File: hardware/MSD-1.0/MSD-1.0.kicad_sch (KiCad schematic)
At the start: 19 parts, among them J1 Conn_01x05, J2 Conn_01x03, Q1 IRF840N, U1 NE555P, U2 PC817, U3 PC817

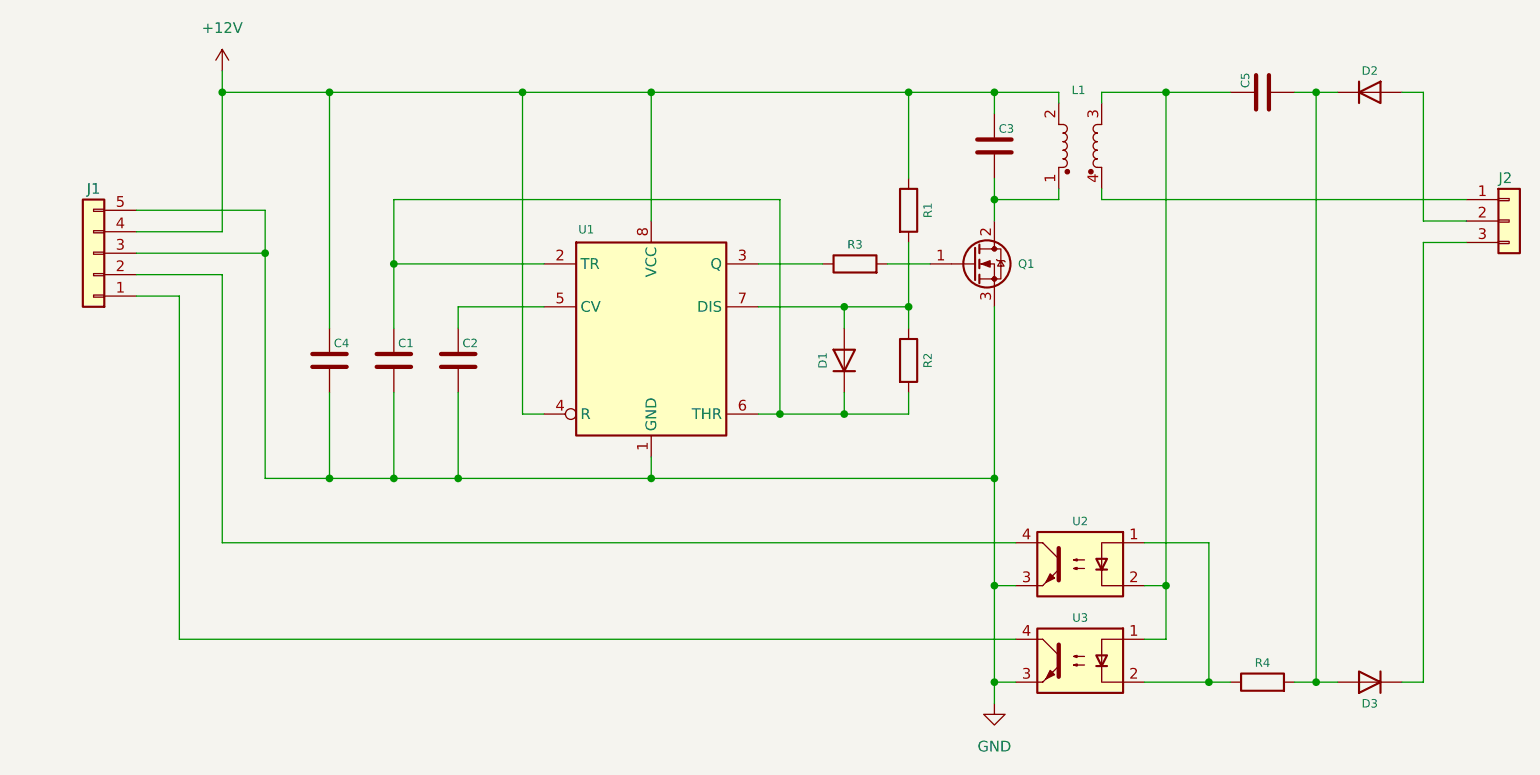
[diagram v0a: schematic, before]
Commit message: deleted:    hardware/MSD-1.0/#auto_saved_files# 	new file:   hardware/MSD-1.0/MSD-1.0 BoM.csv 	new file:   hardware/MSD-1.0/MSD-1.0-B_Cu.gbr 	new file:   hardware/MSD-1.0/MSD-1.0-B_Mask.gbr 	new file:   hardware/MSD-1.0/MSD-1.0-B_Paste.gbr 	new file:   hardware/MSD-1.0/MSD-1.0-B_Silkscreen.gbr 	new file:   hardware/MSD-1.0/MSD-1.0-Edge_Cuts.gbr 	new file:   hardware/MSD-1.0/MSD-1.0-F_Cu.gbr 	new file:   hardware/MSD-1.0/MSD-1.0-F_Mask.gbr 	new file:   hardware/MSD-1.0/MSD-1.0-F_Paste.gbr 	new file:   hardware/MSD-1.0/MSD-1.0-F_Silkscreen.gbr 	new file:   hardware/MSD-1.0/MSD-1.0-NPTH.drl 	new file:   hardware/MSD-1.0/MSD-1.0-PTH.drl 	deleted:    hardware/MSD-1.0/MSD-1.0-backups/MSD-1.0-2025-02-24_160102.zip 	deleted:    hardware/MSD-1.0/MSD-1.0-backups/MSD-1.0-2025-02-24_160721.zip 	deleted:    hardware/MSD-1.0/MSD-1.0-backups/MSD-1.0-2025-02-24_161316.zip 	deleted:    hardware/MSD-1.0/MSD-1.0-backups/MSD-1.0-2025-02-24_162407.zip 	deleted:    hardware/MSD-1.0/MSD-1.0-backups/MSD-1.0-2025-02-24_163137.zip 	deleted:    hardware/MSD-1.0/MSD-1.0-backups/MSD-1.0-2025-02-25_161045.zip 	deleted:    hardware/MSD-1.0/MSD-1.0-backups/MSD-1.0-2025-02-26_093224.zip 	deleted:    hardware/MSD-1.0/MSD-1.0-backups/MSD-1.0-2025-02-26_094218.zip 	new file:   hardware/MSD-1.0/MSD-1.0-backups/MSD-1.0-2025-02-26_163854.zip 	new file:   hardware/MSD-1.0/MSD-1.0-backups/MSD-1.0-2025-02-27_112851.zip 	new file:   hardware/MSD-1.0/MSD-1.0-backups/MSD-1.0-2025-02-27_114053.zip 	new file:   hardware/MSD-1.0/MSD-1.0-backups/MSD-1.0-2025-02-27_185834.zip 	new file:   hardware/MSD-1.0/MSD-1.0-backups/MSD-1.0-2025-02-27_190654.zip 	new file:   hardware/MSD-1.0/MSD-1.0-backups/MSD-1.0-2025-02-27_191228.zip 	new file:   hardware/MSD-1.0/MSD-1.0-backups/MSD-1.0-2025-02-28_140545.zip 	new file:   hardware/MSD-1.0/MSD-1.0-backups/MSD-1.0-2025-02-28_141533.zip 	new file:   hardware/MSD-1.0/MSD-1.0-backups/MSD-1.0-2025-02-28_142536.zip 	new file:   hardware/MSD-1.0/MSD-1.0-backups/MSD-1.0-2025-02-28_14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
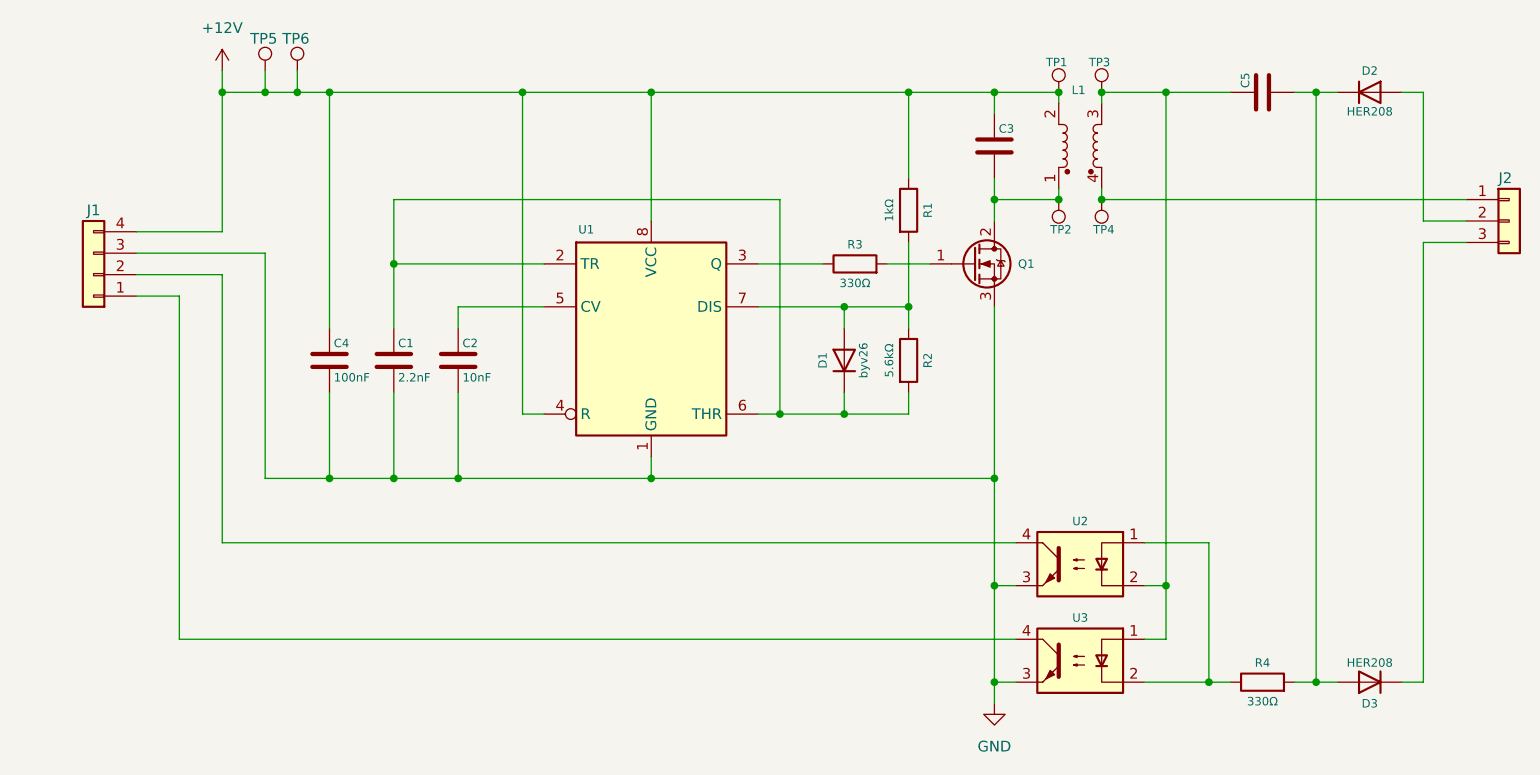
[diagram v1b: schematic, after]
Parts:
- added TP1, TP2, TP3, TP4: TestPoint, TestPoint:TestPoint_Bridge_Pitch2.54mm_Drill1.0mm, symbol Connector:TestPoint
- added TP5, TP6: TestPoint, TestPoint:TestPoint_THTPad_2.0x2.0mm_Drill1.0mm_NoSilkscreen, symbol Connector:TestPoint
- C2: value 470pF -> 10nF
- C3: value 0.022uF 275V MKP -> 0.022uF 400V MKP
- C4: value C -> 100nF
- C5: value 10nF -> ~; footprint Capacitor_THT:C_Rect_L7.0mm_W3.5mm_P5.00mm -> Capacitor_THT:C_Rect_L13.0mm_W5.0mm_P10.00mm_FKS3_FKP3_MKS4
- D2, D3: value D -> HER208
- J1: footprint Connector_PinHeader_2.54mm:PinHeader_1x05_P2.54mm_Horizontal -> Connector_PinHeader_2.54mm:PinHeader_1x04_P2.54mm_Horizontal_Custom; symbol Connector_Generic:Conn_01x05 -> Connector_Generic:Conn_01x04
- J2: footprint Connector_PinHeader_2.54mm:PinHeader_1x03_P5.08mm_Horizontal -> Connector_PinHeader_2.54mm:PinHeader_1x03_P5.08mm_Horizontal_Custom
- L1: value L_Coupled -> Isolation Transformer (Custom)
- Q1: value IRF840N -> IRF840
- R1: value 10kΩ -> 1kΩ
- R4: value R -> 330Ω
- U1: footprint Package_DIP:DIP-8_W7.62mm -> Package_DIP:DIP-8_W7.62mm_Socket
- U2, U3: footprint Package_DIP:DIP-4_W7.62mm -> Package_DIP:DIP-4_W7.62mm_Socket
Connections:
- net +12V: now also TP1.1, TP5.1, TP6.1
- net GND: no longer J1.5 (Pin_5)
- net at C3.2, L1.1, Q1.2 (D): now also TP2.1
- net at J2.1 (Pin_1), L1.4: now also TP4.1
- net at C5.1, L1.3, U2.2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: now also TP3.1

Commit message: modified:   .DS_Store 	deleted:    hardware/MSD-1.0/MSD-1.0-backups/MSD-1.0-2025-02-25_161819.zip 	deleted:    hardware/MSD-1.0/MSD-1.0-backups/MSD-1.0-2025-02-25_162448.zip 	deleted:    hardware/MSD-1.0/MSD-1.0-backups/MSD-1.0-2025-02-25_163016.zip 	deleted:    hardware/MSD-1.0/MSD-1.0-backups/MSD-1.0-2025-02-25_163954.zip 	deleted:    hardware/MSD-1.0/MSD-1.0-backups/MSD-1.0-2025-02-26_112856.zip 	deleted:    hardware/MSD-1.0/MSD-1.0-backups/MSD-1.0-2025-02-26_113923.zip 	deleted:    hardware/MSD-1.0/MSD-1.0-backups/MSD-1.0-2025-02-26_115654.zip 	deleted:    hardware/MSD-1.0/MSD-1.0-backups/MSD-1.0-2025-02-26_120757.zip 	deleted:    hardware/MSD-1.0/MSD-1.0-backups/MSD-1.0-2025-02-26_163854.zip 	deleted:    hardware/MSD-1.0/MSD-1.0-backups/MSD-1.0-2025-02-27_112851.zip 	deleted:    hardware/MSD-1.0/MSD-1.0-backups/MSD-1.0-2025-02-27_114053.zip 	deleted:    hardware/MSD-1.0/MSD-1.0-backups/MSD-1.0-2025-02-27_185834.zip 	deleted:    hardware/MSD-1.0/MSD-1.0-backups/MSD-1.0-2025-02-27_190654.zip 	deleted:    hardware/MSD-1.0/MSD-1.0-backups/MSD-1.0-2025-02-27_191228.zip 	deleted:    hardware/MSD-1.0/MSD-1.0-backups/MSD-1.0-2025-02-28_140545.zip 	deleted:    hardware/MSD-1.0/MSD-1.0-backups/MSD-1.0-2025-02-28_141533.zip 	deleted:    hardware/MSD-1.0/MSD-1.0-backups/MSD-1.0-2025-02-28_142536.zip 	deleted:    hardware/MSD-1.0/MSD-1.0-backups/MSD-1.0-2025-02-28_143342.zip 	deleted:    hardware/MSD-1.0/MSD-1.0-backups/MSD-1.0-2025-02-28_162722.zip 	deleted:    hardware/MSD-1.0/MSD-1.0-backups/MSD-1.0-2025-03-05_134102.zip 	deleted:    hardware/MSD-1.0/MSD-1.0-backups/MSD-1.0-2025-03-05_134620.zip 	new file:   hardware/MSD-1.0/MSD-1.0-backups/MSD-1.0-2025-03-24_113503.zip 	new file:   hardware/MSD-1.0/MSD-1.0-backups/MSD-1.0-2025-03-24_114029.zip 	new file:   hardware/MSD-1.0/MSD-1.0-backups/MSD-1.0-2025-03-24_132745.zip 	new file:   hardware/MSD-1.0/MSD-1.0-backups/MSD-1.0-2025-03-24_134332.zip 	new file:   hardware/MSD-1.0/MSD-1.0-backups/MSD-1.0-2025-03-25_144744.zip 	n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
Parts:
- removed L1: Isolation Transformer (Custom), Inductor_THT:L_CommonMode_Toroid_Vertical_L30.5mm_W15.2mm_Px10.16mm_Py20.32mm_Bourns_8100, symbol Device:L_Coupled_1243
- added C6: 470µF 35V, Capacitor_THT:CP_Radial_D12.5mm_P5.00mm, symbol Device:C_Polarized
- added L1: L_Ferrite_Coupled, Inductor_THT:L_CommonMode_Toroid_Horizontal_OD23mm_ID14mm_H8mm, symbol Device:L_Ferrite_Coupled_1243
- D1: footprint Diode_THT:D_DO-34_SOD68_P7.62mm_Horizontal -> Diode_THT:D_DO-35_SOD27_P7.62mm_Horizontal
- J1: footprint Connector_PinHeader_2.54mm:PinHeader_1x04_P2.54mm_Horizontal_Custom -> Connector_PinHeader_2.54mm:PinHeader_1x04_P2.54mm_Horizontal_2
- J2: footprint Connector_PinHeader_2.54mm:PinHeader_1x03_P5.08mm_Horizontal_Custom -> Connector_PinHeader_2.54mm:PinHeader_1x03_P5.08mm_Horizontal_2
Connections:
- net +12V: now also C6.1, L1.2
- net GND: now also C6.2
- net at C3.2, Q1.2 (D), TP2.1: now also L1.1
- net at J2.1 (Pin_1), TP4.1: now also L1.4
- net at C5.1, TP3.1, U2.2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: now also L1.3
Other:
- moved on the sheet: J1, TP1, TP2, TP3, TP4, TP6

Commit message: new file:   hardware/Gain/Gain-B_Cu.gbr 	new file:   hardware/Gain/Gain-B_Mask.gbr 	new file:   hardware/Gain/Gain-B_Paste.gbr 	new file:   hardware/Gain/Gain-B_Silkscreen.gbr 	new file:   hardware/Gain/Gain-Edge_Cuts.gbr 	new file:   hardware/Gain/Gain-F_Cu.gbr 	new file:   hardware/Gain/Gain-F_Mask.gbr 	new file:   hardware/Gain/Gain-F_Paste.gbr 	new file:   hardware/Gain/Gain-F_Silkscreen.gbr 	new file:   hardware/Gain/Gain-NPTH.drl 	new file:   hardware/Gain/Gain-PTH.drl 	new file:   hardware/Gain/Gain-backups/Gain-2025-04-14_115147.zip 	new file:   hardware/Gain/Gain-backups/Gain-2025-04-14_121847.zip 	new file:   hardware/Gain/Gain-backups/Gain-2025-04-14_133755.zip 	new file:   hardware/Gain/Gain-backups/Gain-2025-04-14_141907.zip 	new file:   hardware/Gain/Gain-backups/Gain-2025-04-14_162042.zip 	new file:   hardware/Gain/Gain-backups/Gain-2025-04-14_163456.zip 	new file:   hardware/Gain/Gain-job.gbrjob 	new file:   hardware/Gain/Gain.kicad_pcb 	new file:   hardware/Gain/Gain.kicad_prl 	new file:   hardware/Gain/Gain.kicad_pro 	new file:   hardware/Gain/Gain.kicad_sch 	new file:   hardware/Gain/Gain.step 	new file:   hardware/Gain/REM-2.0 BoM.csv 	new file:   hardware/Gain/REM-2.0-backups/REM-2.0-2025-03-05_160217.zip 	new file:   hardware/Gain/REM-2.0-backups/REM-2.0-2025-03-06_081735.zip 	new file:   hardware/Gain/REM-2.0-backups/REM-2.0-2025-03-17_111724.zip 	new file:   hardware/Gain/REM-2.0-backups/REM-2.0-2025-03-17_135033.zip 	new file:   hardware/Gain/REM-2.0-backups/REM-2.0-2025-03-18_104019.zip 	new file:   hardware/Gain/REM-2.0-backups/REM-2.0-2025-03-18_141720.zip 	new file:   hardware/Gain/REM-2.0-backups/REM-2.0-2025-03-18_202240.zip 	new file:   hardware/Gain/REM-2.0-backups/REM-2.0-2025-03-18_203414.zip 	new file:   hardware/Gain/REM-2.0-backups/REM-2.0-2025-03-18_204444.zip 	new file:   hardware/Gain/REM-2.0-backups/REM-2.0-2025-03-24_102406.zip 	new file:   hardware/Gain/REM-2.0-backups/REM-2.0-2025-03-24_103843.zip 	new file:   hardware/Ga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
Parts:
- C5: value ~ -> 100nF 400V
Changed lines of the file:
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@@
 			)
 		)
-		(property "Value" "~"
+		(property "Value" "100nF 400V"
 			(at 167.132 31.242 0)
 			(effects
@@
 				)
 				(justify left)
+				(hide yes)
 			)
 		)

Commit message: deleted:    hardware/Gain/Gain-backups/Gain-2025-04-14_115147.zip 	new file:   hardware/Gain/Gain-backups/Gain-2025-04-15_120154.zip 	deleted:    hardware/MSD-1.0/MSD-1.0-backups/MSD-1.0-2025-03-24_134332.zip 	deleted:    hardware/MSD-1.0/MSD-1.0-backups/MSD-1.0-2025-03-25_144744.zip 	deleted:    hardware/MSD-1.0/MSD-1.0-backups/MSD-1.0-2025-03-25_145433.zip 	deleted:    hardware/MSD-1.0/MSD-1.0-backups/MSD-1.0-2025-03-25_150210.zip 	deleted:    hardware/MSD-1.0/MSD-1.0-backups/MSD-1.0-2025-03-25_150818.zip 	new file:   hardware/MSD-1.0/MSD-1.0-backups/MSD-1.0-2025-04-16_142822.zip 	new file:   hardware/MSD-1.0/MSD-1.0-backups/MSD-1.0-2025-04-16_143722.zip 	new file:   hardware/MSD-1.0/MSD-1.0-backups/MSD-1.0-2025-04-16_145208.zip 	new file:   hardware/MSD-1.0/MSD-1.0-backups/MSD-1.0-2025-04-16_150237.zip 	new file:   hardware/MSD-1.0/MSD-1.0-backups/MSD-1.0-2025-04-16_150829.zip 	modified:   hardware/MSD-1.0/MSD-1.0.kicad_pcb 	modified:   hardware/MSD-1.0/MSD-1.0.kicad_sch 	modified:   hardware/MSD-1.0/MSD-1.0.step 	new file:   hardware/MSD-2.0/MSD-2.0-backups/MSD-2.0-2025-04-16_090248.zip 	deleted:    hardware/PS-1.0/PS-1.0-backups/PS-1.0-2025-03-18_205016.zip 	deleted:    hardware/PS-1.0/PS-1.0-backups/PS-1.0-2025-03-18_205728.zip 	deleted:    hardware/PS-1.0/PS-1.0-backups/PS-1.0-2025-03-18_211157.zip 	deleted:    hardware/PS-1.0/PS-1.0-backups/PS-1.0-2025-03-18_213933.zip 	deleted:    hardware/PS-1.0/PS-1.0-backups/PS-1.0-2025-03-19_094557.zip 	deleted:    hardware/PS-1.0/PS-1.0-backups/PS-1.0-2025-03-19_101204.zip 	deleted:    hardware/PS-1.0/PS-1.0-backups/PS-1.0-2025-03-19_102323.zip 	new file:   hardware/PS-1.0/PS-1.0-backups/PS-1.0-2025-04-16_154157.zip 	new file:   hardware/PS-1.0/PS-1.0-backups/PS-1.0-2025-04-16_154838.zip 	new file:   hardware/PS-1.0/PS-1.0-backups/PS-1.0-2025-04-16_155906.zip 	new file:   hardware/PS-1.0/PS-1.0-backups/PS-1.0-2025-04-16_160456.zip 	new file:   hardware/PS-1.0/PS-1.0-backups/PS-1.0-2025-04-16_161300.zip 	new file:   har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
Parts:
- added TP7: TestPoint, TestPoint:TestPoint_Bridge_Pitch2.54mm_Drill1.0mm, symbol Connector:TestPoint
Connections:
- net GND: now also TP7.1
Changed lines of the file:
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@@
+	)
+	(junction
+		(at 39.37 50.8)
+		(diameter 0)
+		(color 0 0 0 0)
 	)
 	(junction
@@
 		(pts
 			(xy 153.67 90.17) (xy 153.67 96.52)
+		)
+		(stroke
+			(width 0)
+			(type default)
+		)
+	)
+	(wire
+		(pts
+			(xy 39.37 29.21) (xy 39.37 50.8)
 		)
 		(stroke
@@
 					(unit 1)
 				)
+			)
+		)
+	)
+	(symbol
+		(lib_id "Connector:TestPoint")
+		(at 39.37 29.21 0)
+		(unit 1)
+		(exclude_from_sim no)
+		(in_bom yes)
+		(on_board yes)
+		(dnp no)
+		(property "Reference" "TP7"
+			(at 37.846 25.654 0)
+			(effects
+				(font
+					(size 1 1)
+				)
+				(justify left)
+			)
+		)
+		(property "Value" "TestPoint"
+			(at 41.91 28.4479 0)
+			(effects
+				(font
+					(size 1 1)
+				)
+				(justify left)
+				(hide yes)
+			)
+		)
+		(property "Footprint" "TestPoint:TestPoint_Bridge_Pitch2.54mm_Drill1.0mm"
+			(at 44.45 29.21 0)
+			(effects
+				(font
+					(size 1.27 1.27)
+				)
+				(hide yes)
+			)
+		)
+		(property "Datasheet" "~"
+			(at 44.45 29.21 0)
+			(effects
+				(font
+					(size 1.27 1.27)
+				)
+				(hide yes)
+			)
+		)
+		(property "Description" "test point"
+			(at 39.37 29.21 0)
+			(effects
+				(font
+					(size 1.27 1.27)
+				)
+				(hide yes)
+			)
+		)
+		(pin "1"
+		)
+		(instances
+			(project "MSD-1.0"
+				(path "/c4b28516-96bf-4ad5-83fa-fa81b3e93272"
+					(reference "TP7")
+					(unit 1)
+				)

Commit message: new file:   .~BoM.xlsx 	new file:   BoM.xlsx 	new file:   hardware/BoM.xlsx 	deleted:    hardware/MSD-1.0/MSD-1.0-backups/MSD-1.0-2025-03-26_092035.zip 	deleted:    hardware/MSD-1.0/MSD-1.0-backups/MSD-1.0-2025-03-26_092834.zip 	deleted:    hardware/MSD-1.0/MSD-1.0-backups/MSD-1.0-2025-03-27_092014.zip 	new file:   hardware/MSD-1.0/MSD-1.0-backups/MSD-1.0-2025-04-28_130614.zip 	new file:   hardware/MSD-1.0/MSD-1.0-backups/MSD-1.0-2025-04-28_131128.zip 	new file:   hardware/MSD-1.0/MSD-1.0-backups/MSD-1.0-2025-04-28_132753.zip 	new file:   hardware/MSD-1.0/MSD-1.0.csv 	modified:   hardware/MSD-1.0/MSD-1.0.kicad_pcb 	modified:   hardware/MSD-1.0/MSD-1.0.kicad_sch 	deleted:    hardware/PS-1.0/PS-1.0-backups/PS-1.0-2025-03-24_111800.zip 	deleted:    hardware/PS-1.0/PS-1.0-backups/PS-1.0-2025-03-24_112738.zip 	deleted:    hardware/PS-1.0/PS-1.0-backups/PS-1.0-2025-03-25_152833.zip 	deleted:    hardware/PS-1.0/PS-1.0-backups/PS-1.0-2025-03-25_154601.zip 	deleted:    hardware/PS-1.0/PS-1.0-backups/PS-1.0-2025-03-25_155821.zip 	deleted:    hardware/PS-1.0/PS-1.0-backups/PS-1.0-2025-04-11_101418.zip 	deleted:    hardware/PS-1.0/PS-1.0-backups/PS-1.0-2025-04-11_110528.zip 	deleted:    hardware/PS-1.0/PS-1.0-backups/PS-1.0-2025-04-11_111527.zip 	deleted:    hardware/PS-1.0/PS-1.0-backups/PS-1.0-2025-04-11_114252.zip 	deleted:    hardware/PS-1.0/PS-1.0-backups/PS-1.0-2025-04-17_105409.zip 	new file:   hardware/PS-1.0/PS-1.0-backups/PS-1.0-2025-04-19_071925.zip 	new file:   hardware/PS-1.0/PS-1.0-backups/PS-1.0-2025-04-27_222808.zip 	new file:   hardware/PS-1.0/PS-1.0-backups/PS-1.0-2025-04-27_223939.zip 	new file:   hardware/PS-1.0/PS-1.0-backups/PS-1.0-2025-04-27_224445.zip 	new file:   hardware/PS-1.0/PS-1.0-backups/PS-1.0-2025-04-27_225206.zip 	new file:   hardware/PS-1.0/PS-1.0-backups/PS-1.0-2025-04-27_230217.zip 	new file:   hardware/PS-1.0/PS-1.0-backups/PS-1.0-2025-04-28_083014.zip 	new file:   hardware/PS-1.0/PS-1.0-backups/PS-1.0-2025-04-28_112951.zip 	new file:   har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
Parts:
- C1: value 2.2nF -> 2.2nF 100
- C2: value 10nF -> 10nF 63
- C3: value 0.022uF 400V MKP -> 0.022µF 400
- C4: value 100nF -> 100nF 100
- C5: value 100nF 400V -> 0.1µF 400
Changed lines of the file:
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@@
 			)
 		)
-		(property "Value" "0.022uF 400V MKP"
+		(property "Value" "0.022µF 400"
 			(at 133.858 40.132 0)
 			(effects
@@
 			)
 		)
-		(property "Value" "2.2nF"
+		(property "Value" "2.2nF 100"
 			(at 62.738 65.532 0)
 			(effects
@@
 			)
 		)
-		(property "Value" "100nF"
+		(property "Value" "100nF 100"
 			(at 55.118 65.532 0)
 			(effects
@@
 			)
 		)
-		(property "Value" "100nF 400V"
+		(property "Value" "0.1µF 400"
 			(at 167.132 31.242 0)
 			(effects
@@
 			)
 		)
-		(property "Value" "10nF"
+		(property "Value" "10nF 63"
 			(at 70.358 65.532 0)
 			(effects

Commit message: modified:   .DS_Store 	modified:   README.md 	deleted:    hardware/MSD-1.0/MSD-1.0 BoM.csv 	deleted:    hardware/MSD-1.0/MSD-1.0-backups/MSD-1.0-2025-04-08_110759.zip 	deleted:    hardware/MSD-1.0/MSD-1.0-backups/MSD-1.0-2025-04-08_111313.zip 	new file:   hardware/MSD-1.0/MSD-1.0-backups/MSD-1.0-2025-05-06_093009.zip 	new file:   hardware/MSD-1.0/MSD-1.0-backups/MSD-1.0-2025-05-06_093605.zip 	modified:   hardware/MSD-1.0/MSD-1.0.kicad_pcb 	modified:   hardware/MSD-1.0/MSD-1.0.kicad_sch 	modified:   hardware/MSD-1.0/fp-info-cache 	deleted:    hardware/PS-1.0/PS-1.0-backups/PS-1.0-2025-04-16_161300.zip 	deleted:    hardware/PS-1.0/PS-1.0-backups/PS-1.0-2025-04-16_162332.zip 	deleted:    hardware/PS-1.0/PS-1.0-backups/PS-1.0-2025-04-16_163259.zip 	deleted:    hardware/PS-1.0/PS-1.0-backups/PS-1.0-2025-04-17_110908.zip 	deleted:    hardware/PS-1.0/PS-1.0-backups/PS-1.0-2025-04-17_114838.zip 	deleted:    hardware/PS-1.0/PS-1.0-backups/PS-1.0-2025-04-17_155117.zip 	new file:   hardware/PS-1.0/PS-1.0-backups/PS-1.0-2025-05-06_094214.zip 	new file:   hardware/PS-1.0/PS-1.0-backups/PS-1.0-2025-05-06_095559.zip 	new file:   hardware/PS-1.0/PS-1.0-backups/PS-1.0-2025-05-06_100430.zip 	new file:   hardware/PS-1.0/PS-1.0-backups/PS-1.0-2025-05-06_100931.zip 	new file:   hardware/PS-1.0/PS-1.0-backups/PS-1.0-2025-05-06_101736.zip 	new file:   hardware/PS-1.0/PS-1.0-backups/PS-1.0-2025-05-06_102708.zip 	modified:   hardware/PS-1.0/PS-1.0.kicad_pcb 	modified:   hardware/PS-1.0/PS-1.0.kicad_sch 	new file:   hardware/PS-2.0/PS-2.0-B_Cu.gbr 	new file:   hardware/PS-2.0/PS-2.0-B_Mask.gbr 	new file:   hardware/PS-2.0/PS-2.0-B_Paste.gbr 	new file:   hardware/PS-2.0/PS-2.0-B_Silkscreen.gbr 	new file:   hardware/PS-2.0/PS-2.0-Edge_Cuts.gbr 	new file:   hardware/PS-2.0/PS-2.0-F_Cu.gbr 	new file:   hardware/PS-2.0/PS-2.0-F_Mask.gbr 	new file:   hardware/PS-2.0/PS-2.0-F_Paste.gbr 	new file:   hardware/PS-2.0/PS-2.0-F_Silkscreen.gbr 	new file:   hardware/PS-2.0/PS-2.0-NPTH.drl 	new file:   har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
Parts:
- C5: footprint Capacitor_THT:C_Rect_L13.0mm_W5.0mm_P10.00mm_FKS3_FKP3_MKS4 -> Capacitor_THT:C_Rect_L19.0mm_W7.0mm_P15.00mm_MKS4
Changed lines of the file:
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@@
 			)
 		)
-		(property "Footprint" "Capacitor_THT:C_Rect_L13.0mm_W5.0mm_P10.00mm_FKS3_FKP3_MKS4"
+		(property "Footprint" "Capacitor_THT:C_Rect_L19.0mm_W7.0mm_P15.00mm_MKS4"
 			(at 168.91 30.7848 0)
 			(effects
